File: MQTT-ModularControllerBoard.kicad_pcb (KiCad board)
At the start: 4 copper layers, 200 x 45 mm, 84 parts, among them IC301 LM74700QDBVTQ1, IC401 TPS563200DDCR, IC402 LM74700QDBVTQ1, J301 1715721, J501 A2541HWV-10P, J502 A2541HWV-10P, J503 A2541HWV-10P, J504 A2541HWV-10P, J505 A2541HWV-10P, J506 A2541HWV-10P, J507 A2541HWV-10P, J508 A2541HWV-10P, J602 1051640001, Q301 60V 38A, Q401 60V 38A, U201 ESP32-S3-WROOM-1U-N16R8, U401 LDO 3.3V 1A, U601 ESD Protection IC

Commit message: Update
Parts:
- added G***: LOGO, LOGO, F.Cu at (53.5, 114.7)
- added G***: LOGO, LOGO, B.Cu at (164.9, 102.3)
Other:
- board text added: "M1"
- board text added: "M2"
- board text added: "M3"
- board text added: "M4"
- board text added: "github.com/WiddleWabbit/ MQTT-ModularControllerBoard"

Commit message: Added Copyright notice to board.
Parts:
- moved G*** 1.41 mm to (163.9, 101.3)
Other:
- board text added: "Licensed under CERN-OHL-P v2"
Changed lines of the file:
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@@
 	(footprint "LOGO"
 		(layer "B.Cu")
-		(at 164.9 102.3 180)
+		(at 163.9 101.3 180)
 		(property "Reference" "G***"
 			(at 0 0 0)
@@
 		)
 	)
+	(gr_text "Licensed under CERN-OHL-P v2"
+		(at 158.8 104.3 0)
+		(layer "B.SilkS")
+		(effects
+			(font
+				(size 1.2 1.2)
+				(thickness 0.3)
+				(bold yes)
+			)
+			(justify left bottom mirror)
+		)
+	)
 	(gr_text "github.com/WiddleWabbit/\nMQTT-ModularControllerBoard"
-		(at 158.5 104.3 0)
+		(at 159.1 101.5 0)
 		(layer "B.SilkS")
 		(effects
 			(font
-				(size 1.3 1.3)
+				(size 1.5 1.5)
 				(thickness 0.325)
 				(bold yes)

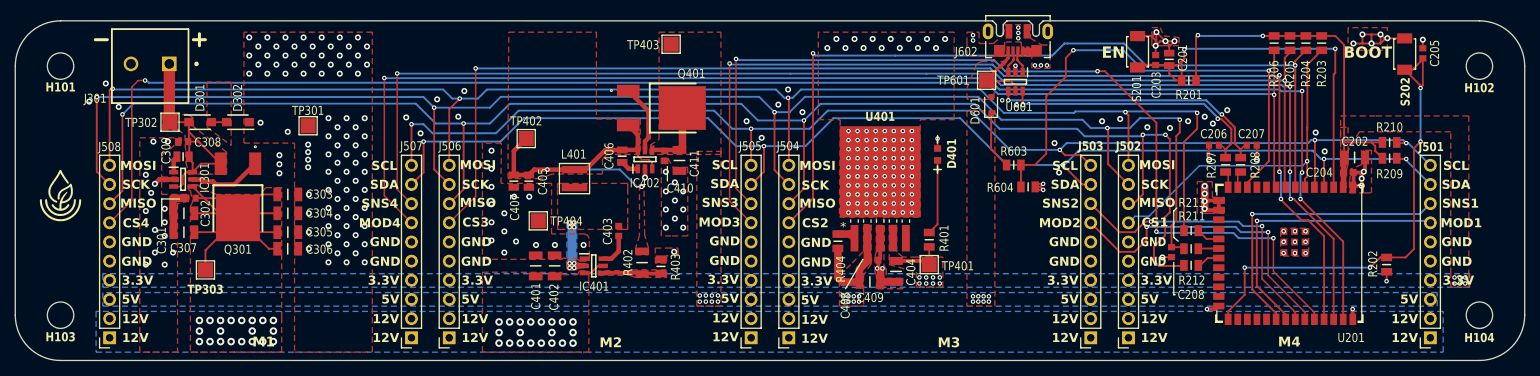
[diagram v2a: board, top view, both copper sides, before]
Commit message: Minor tweaking, increased spacing on close Via's, ensured star routing pattern on a couple of components.
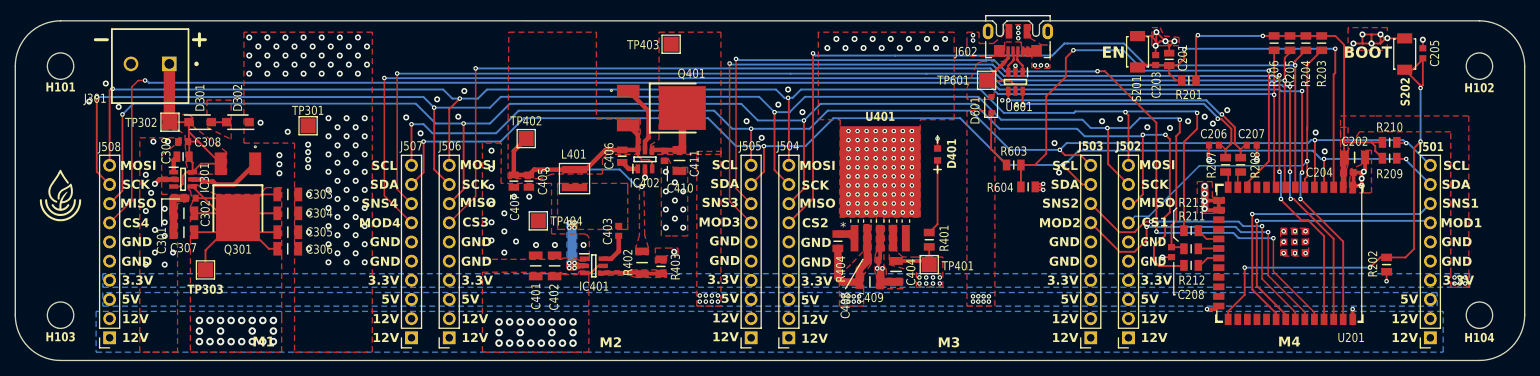
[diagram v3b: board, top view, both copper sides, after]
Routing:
- net /ESP32-S3/EN: track 52.6 -> 50.1 mm
- net Net-(IC401-SW): track 19.1 -> 19.6 mm
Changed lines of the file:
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@@
 	)
 	(segment
-		(start 202.05 99.4)
-		(end 202.05 96.85)
-		(width 0.25)
-		(layer "F.Cu")
-		(net 1)
-	)
-	(segment
 		(start 222.18 98.62)
 		(end 222.18 113.55)
@@
 	)
 	(segment
-		(start 122.898 123.966)
-		(end 121.224 123.966)
+		(start 121.824 123.966)
+		(end 122.898 123.966)
 		(width 0.6)
 		(layer "F.Cu")
@@
 	)
 	(segment
-		(start 121.224 123.966)
-		(end 120.954 124.236)
+		(start 120.964 118.836)
+		(end 120.9 118.9)
 		(width 0.6)
 		(layer "F.Cu")
@@
 	)
 	(segment
-		(start 120.954 118.236)
-		(end 120.954 118.836)
+		(start 120.954 118.782)
+		(end 120.954 118.29)
 		(width 0.6)
 		(layer "F.Cu")
@@
 	)
 	(segment
-		(start 121.554 118.236)
-		(end 120.954 118.236)
+		(start 120.936 123.636)
+		(end 120.954 123.636)
 		(width 0.6)
 		(layer "F.Cu")
@@
 	(segment
 		(start 121.284 123.966)
-		(end 120.954 123.636)
+		(end 122.898 123.966)
+		(width 0.6)
+		(layer "F.Cu")
+		(net 11)
+	)
+	(segment
+		(start 121.6 124.236)
+		(end 121.6 124.19)
+		(width 0.6)
+		(layer "F.Cu")
+		(net 11)
+	)
+	(segment
+		(start 121.6 123.682)
+		(end 121.884 123.966)
+		(width 0.6)
+		(layer "F.Cu")
+		(net 11)
+	)
+	(segment
+		(start 120.954 118.29)
+		(end 120.9 118.236)
+		(width 0.6)
+		(layer "F.Cu")
+		(net 11)
+	)
+	(segment
+		(start 120.9 118.836)
+		(end 120.954 118.782)
+		(width 0.6)
+		(layer "F.Cu")
+		(net 11)
+	)
+	(segment
+		(start 121.554 118.79)
+		(end 121.554 118.282)
+		(width 0.6)
+		(layer "F.Cu")
+		(net 11)
+	)
+	(segment
+		(start 120.9 123.6)
+		(end 120.936 123.636)
+		(width 0.6)
+		(layer "F.Cu")
+		(net 11)
+	)
+	(segment
+		(start 121.6 118.836)
+		(end 121.554 118.79)
+		(width 0.6)
+		(layer "F.Cu")
+		(net 11)
+	)
+	(segment
+		(start 120.9 124.236)
+		(end 120.954 124.236)
+		(width 0.6)
+		(layer "F.Cu")
+		(net 11)
+	)
+	(segment
+		(start 121.554 118.282)
+		(end 121.6 118.236)
 		(width 0.6)
 		(layer "F.Cu")
@@
 	(segment
 		(start 121.884 123.966)
-		(end 121.554 123.636)
+		(end 122.898 123.966)
 		(width 0.6)
 		(layer "F.Cu")
@@
 	)
 	(segment
-		(start 122.898 123.966)
-		(end 121.284 123.966)
+		(start 120.954 124.236)
+		(end 121.224 123.966)
 		(width 0.6)
 		(layer "F.Cu")
@@
 	)
 	(segment
-		(start 120.954 118.836)
-		(end 121.554 118.836)
+		(start 121.6 118.9)
+		(end 121.536 118.836)
 		(width 0.6)
 		(layer "F.Cu")
@@
 	)
 	(segment
-		(start 122.898 123.966)
-		(end 121.824 123.966)
+		(start 121.6 118.236)
+		(end 120.9 118.236)
 		(width 0.6)
 		(layer "F.Cu")
@@
 	)
 	(segment
-		(start 121.554 118.236)
-		(end 121.554 118.836)
+		(start 121.6 118.9)
+		(end 121.6 118.836)
 		(width 0.6)
 		(layer "F.Cu")
@@
 	)
 	(segment
-		(start 121.824 123.966)
-		(end 121.554 124.236)
+		(start 121.6 123.6)
+		(end 121.6 123.682)
 		(width 0.6)
 		(layer "F.Cu")
@@
 	)
 	(segment
-		(start 122.898 123.966)
-		(end 121.884 123.966)
+		(start 121.536 118.836)
+		(end 120.964 118.836)
+		(width 0.6)
+		(layer "F.Cu")
+		(net 11)
+	)
+	(segment
+		(start 120.954 123.636)
+		(end 121.284 123.966)
+		(width 0.6)
+		(layer "F.Cu")
+		(net 11)
+	)
+	(segment
+		(start 121.224 123.966)
+		(end 122.898 123.966)
+		(width 0.6)
+		(layer "F.Cu")
+		(net 11)
+	)
+	(segment
+		(start 120.9 118.9)
+		(end 120.9 118.836)
+		(width 0.6)
+		(layer "F.Cu")
+		(net 11)
+	)
+	(segment
+		(start 121.6 124.19)
+		(end 121.824 123.966)
 		(width 0.6)
 		(layer "F.Cu")
@@
 	)
 	(via
-		(at 120.954 118.836)
+		(at 120.9 118.9)
 		(size 0.6)
 		(drill 0.3)
@@
 	)
 	(via
-		(at 120.954 118.236)
+		(at 120.9 118.236)
 		(size 0.6)
 		(drill 0.3)
@@
 	)
 	(via
-		(at 121.554 124.236)
+		(at 121.6 124.236)
 		(size 0.6)
 		(drill 0.3)
@@
 	)
 	(via
-		(at 121.554 123.636)
+		(at 121.6 123.6)
 		(size 0.6)
 		(drill 0.3)
@@
 	)
 	(via
-		(at 121.554 118.236)
+		(at 121.6 118.236)
 		(size 0.6)
 		(drill 0.3)
@@
 	)
 	(via
-		(at 121.554 118.836)
+		(at 121.6 118.9)
 		(size 0.6)
 		(drill 0.3)
@@
 	)
 	(via
-		(at 120.954 124.236)
+		(at 120.9 124.236)
 		(size 0.6)
 		(drill 0.3)
@@
 	)
 	(via
-		(at 120.954 123.636)
+		(at 120.9 123.6)
 		(size 0.6)
 		(drill 0.3)
@@
 	)
 	(segment
-		(start 121.554 118.836)
-		(end 121.554 123.636)
+		(start 121.564 123.6)
+		(end 121.554 123.59)
 		(width 0.6)
 		(layer "B.Cu")
@@
 	)
 	(segment
-		(start 120.954 118.836)
-		(end 120.954 123.636)
+		(start 120.9 123.6)
+		(end 120.936 123.6)
+		(width 0.6)
+		(layer "B.Cu")
+		(net 11)
+	)
+	(segment
+		(start 120.954 123.582)
+		(end 120.954 118.954)
+		(width 0.6)
+		(layer "B.Cu")
+		(net 11)
+	)
+	(segment
+		(start 120.954 118.954)
+		(end 120.9 118.9)
+		(width 0.6)
+		(layer "B.Cu")
+		(net 11)
+	)
+	(segment
+		(start 121.554 123.59)
+		(end 121.554 118.946)
+		(width 0.6)
+		(layer "B.Cu")
+		(net 11)
+	)
+	(segment
+		(start 120.936 123.6)
+		(end 120.954 123.582)
+		(width 0.6)
+		(layer "B.Cu")
+		(net 11)
+	)
+	(segment
+		(start 121.6 123.6)
+		(end 121.564 123.6)
+		(width 0.6)
+		(layer "B.Cu")
+		(net 11)
+	)
+	(segment
+		(start 121.554 118.946)
+		(end 121.6 118.9)
 		(width 0.6)
 		(layer "B.Cu")
@@
 		(polygon
 			(pts
-				(xy 72.9 105.6) (xy 76.1 108) (xy 76.1 99.6) (xy 72.9 99.6)
+				(xy 72.9 105.6) (xy 76.1 107.2) (xy 76.1 102) (xy 72.9 102)
 			)
 		)

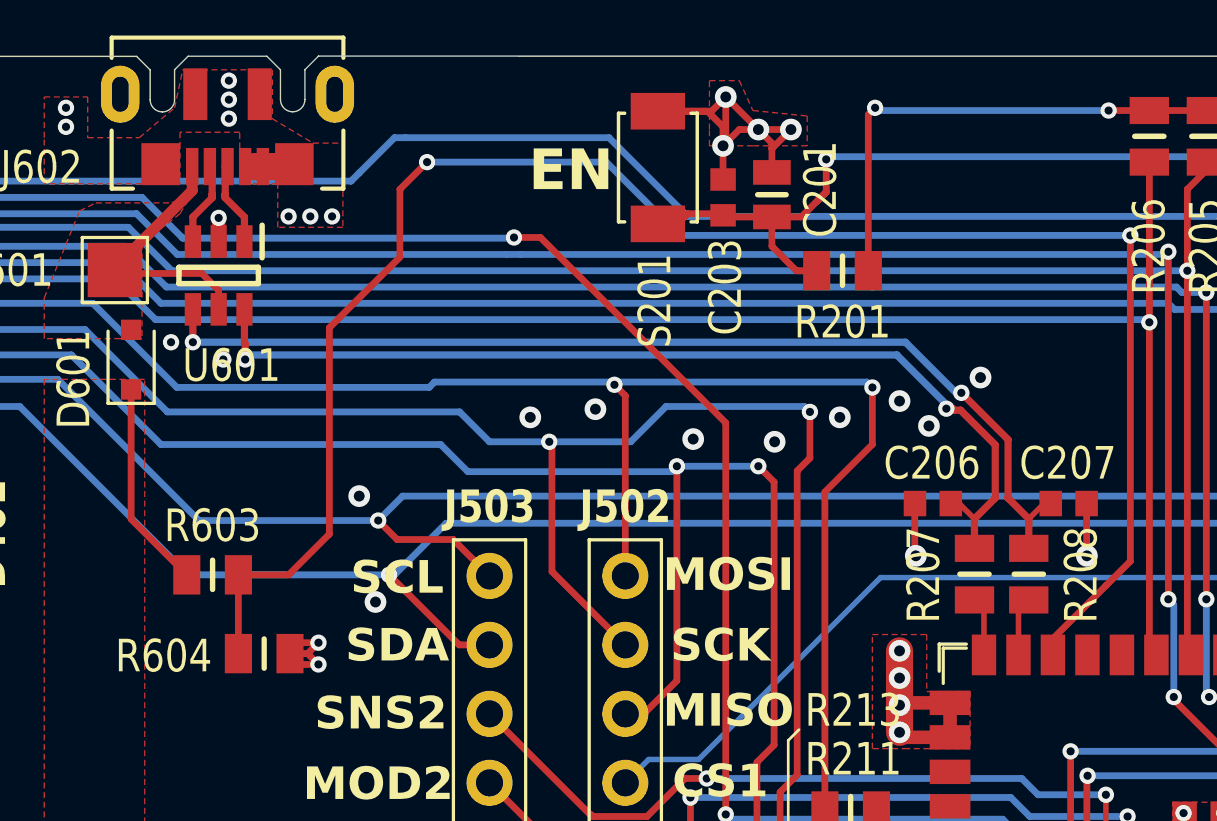
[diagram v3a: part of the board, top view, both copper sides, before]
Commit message: Recalculated and reran the USB Lines and impedance. Updated symbols to work in BOM. Ran output.
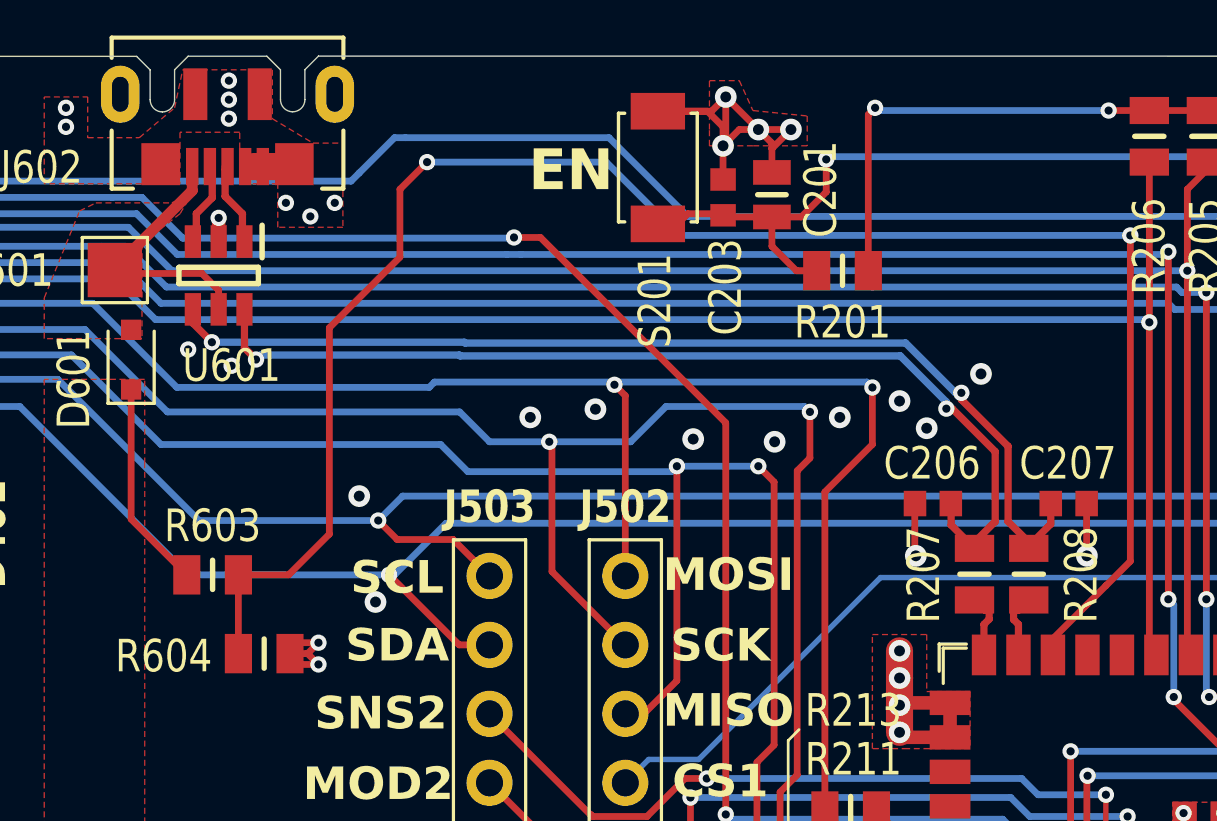
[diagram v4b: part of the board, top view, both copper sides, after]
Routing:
- net /ESP32-S3/D_R+: track 36.5 -> 37.0 mm

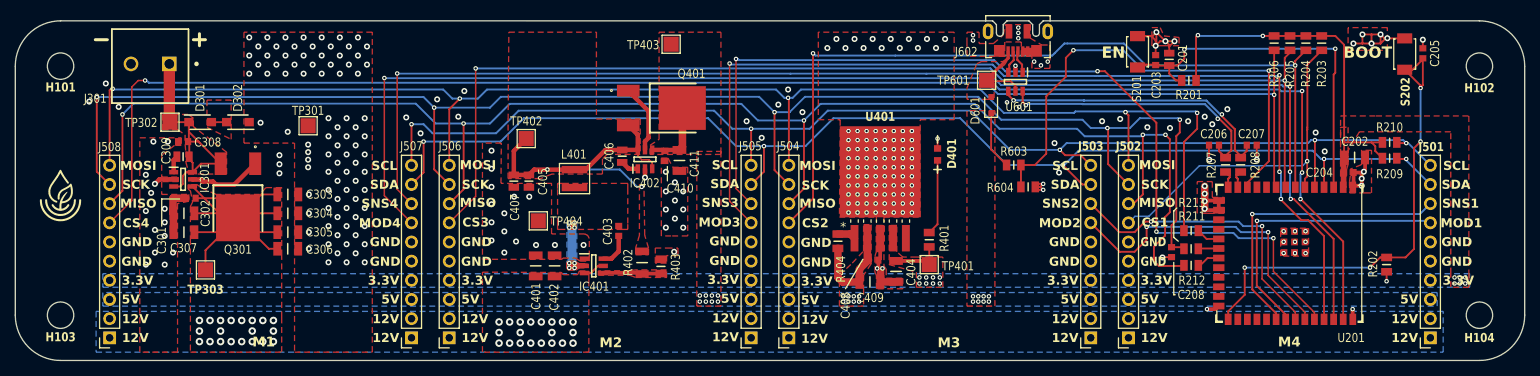
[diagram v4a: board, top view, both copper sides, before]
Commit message: Updated inductor component and 10uF capacitor components to bring down cost.
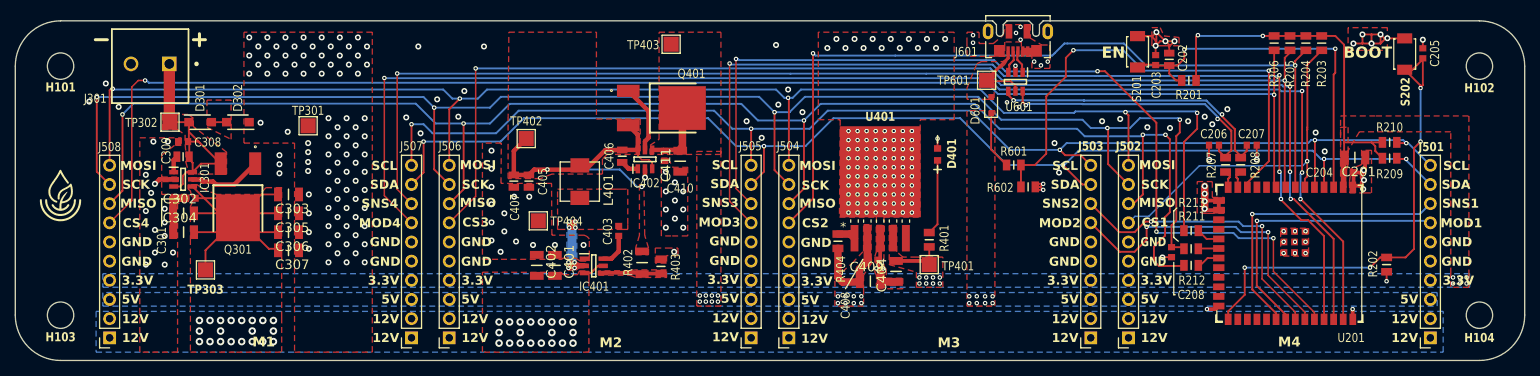
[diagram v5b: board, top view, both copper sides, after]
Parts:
- removed the C202 at (225.0, 109.6)
- added C201: 10uF 10% 25V, JLCPCB Basic:CAPC3216X180N, F.Cu at (225.0, 109.6)
- C302, C303, C304, C305, C306, C307, C401, C402, C404, C409, C411: value 10uF 10% 50V -> 10uF 10% 25V
- H101, H102, H103, H104: value 3.5mm -> MountingHole 3.5mm
- L401: value 3.3uH 6.6A 20% -> 3.3uH 6.3A 20%; footprint COILCRAFT Inductors:XAL40XX -> KOHERELEC Inductors:SMD57x52mm
- S201, S202: value SPST -> Push Button SPST
- moved C307 14.1 mm to (83.7, 121.9), turned to 180 degrees
- moved C304 14.0 mm to (69.8, 119.5), turned to 0 degrees
- moved C401 2.54 mm to (119.0, 123.9), turned to -90 degrees
- moved C305 2.50 mm to (83.7, 117.0)
- moved C402 2.36 mm to (116.6, 123.9), turned to -90 degrees
- moved C306 2.20 mm to (83.7, 119.5)
- moved L401 0.81 mm to (122.3, 112.8)
- moved C411 0.14 mm to (135.6, 110.1)
- moved C409 0.12 mm to (160.8, 126.0), turned to 0 degrees
- moved C303 0.09 mm to (83.7, 114.5)
- turned C404 to 90 degrees
- renumbered C201 to C202, J602 to J601, R603 to R601, R604 to R602
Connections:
- C401 pad 1: +12V -> GND
- C401 pad 2: GND -> +12V
- C402 pad 1: +12V -> GND
- C402 pad 2: GND -> +12V
- C404 pad 1: +3V3 -> GND
- C404 pad 2: GND -> +3V3
- C409 pad 1: GND -> +5V
- C409 pad 2: +5V -> GND
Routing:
- net GND: track 85.7 -> 87.2 mm, vias 298 -> 301
- net Net-(IC401-SW): track 19.6 -> 20.7 mm
